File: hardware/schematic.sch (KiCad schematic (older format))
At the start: 12 parts

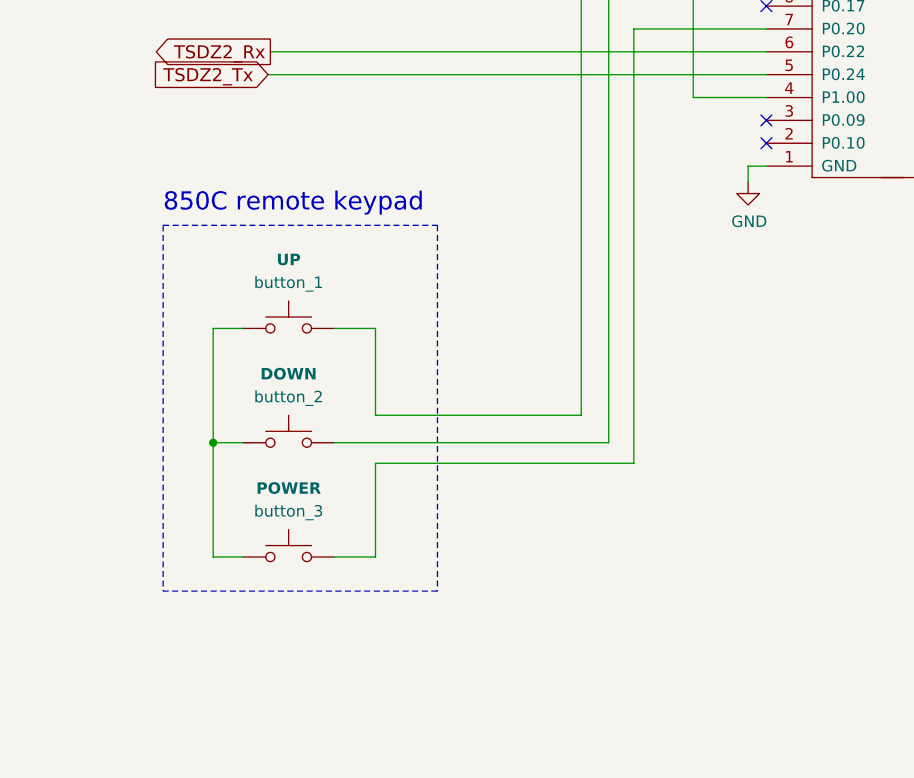
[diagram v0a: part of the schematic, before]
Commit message: WIP display and buttons work
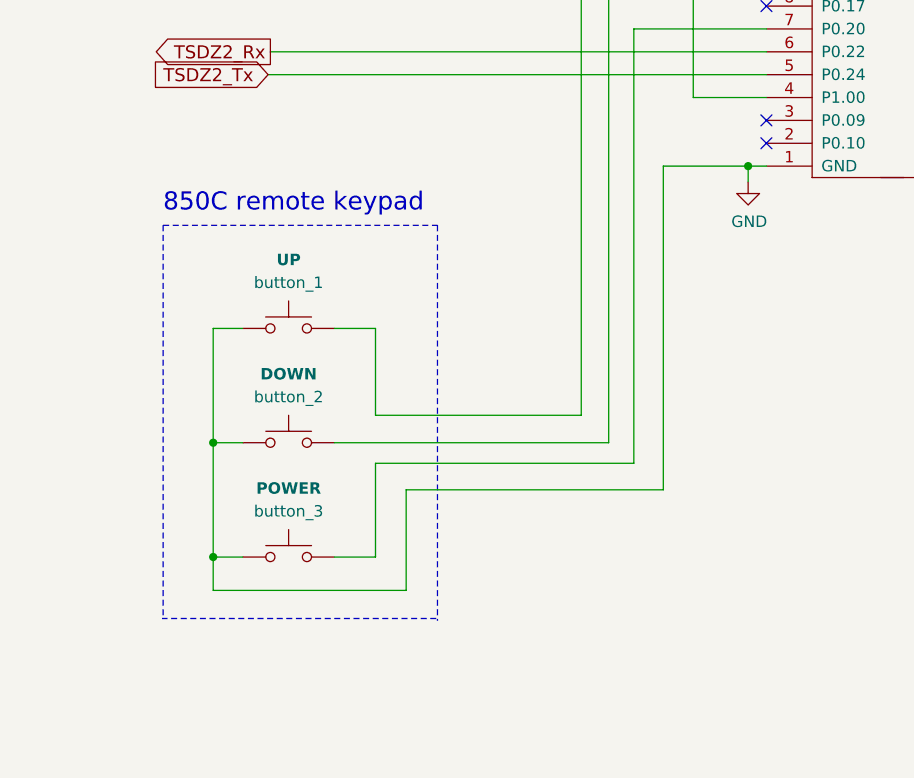
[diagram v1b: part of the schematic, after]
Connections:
- net GND: now also button_1.1, button_2.1, button_3.1
- net at U?.2 (VDD_out): now also Brd?.2 (VCC)
- net at U?.4 (P1.00): now also U?.1
- net at U?.8 (P1.13): now also Brd?.4 (SDA)
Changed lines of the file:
@@
 	7737 5623 8937 5623
 Wire Notes Line
-	8937 5623 8937 7223
-Wire Notes Line
-	8937 7223 7737 7223
+	8937 5623 8937 7353
+Wire Notes Line
+	8932 7343 7732 7343
 Text Notes 7737 5573 0    79   ~ 0
 850C remote keypad
@@
 TSDZ2_5V
 Wire Notes Line
-	7737 5623 7737 7223
+	7737 5623 7737 7343
 $Comp
 L Wired_remote:Switch_SW_Push button_3
@@
 	7956 6574 8086 6574
 Wire Wire Line
-	7956 6574 7956 7074
-Wire Wire Line
 	7956 7074 8086 7074
 Connection ~ 7956 6574
@@
 Wire Wire Line
 	4099 7629 5214 7629
+Wire Wire Line
+	7956 7220 8800 7220
+Wire Wire Line
+	8800 7220 8800 6780
+Wire Wire Line
+	8800 6780 9925 6780
+Wire Wire Line
+	9925 6780 9925 5364
+Wire Wire Line
+	9925 5364 10296 5364
+Wire Wire Line
+	7956 6574 7956 7074
+Connection ~ 7956 7074
+Wire Wire Line
+	7956 7074 7956 7220
+Connection ~ 10296 5364
 $EndSCHEMATC
